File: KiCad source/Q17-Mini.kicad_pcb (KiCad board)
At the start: 2 copper layers, 95 x 75 mm, 85 parts, among them J1 Input, J2-1 SPK+, J2-2 SPK-, J3-1 V+, J3-2 GND, J3-3 V-, Q1 IRF610, Q10 KSA992, Q11 BS250P, Q12 BD139, Q13 IRF610, Q14 IRF9610, Q15 FQA46N15, Q16 FQA36P15, Q2 KSA992, Q3 KSC1845, Q4 IRF9610, Q5 FQP3P20, Q6 FQP3N30, Q7 KSC1845, Q8 ZVN4206AV, Q9 BS250P, U1 OPA1641, U1' OPA1641

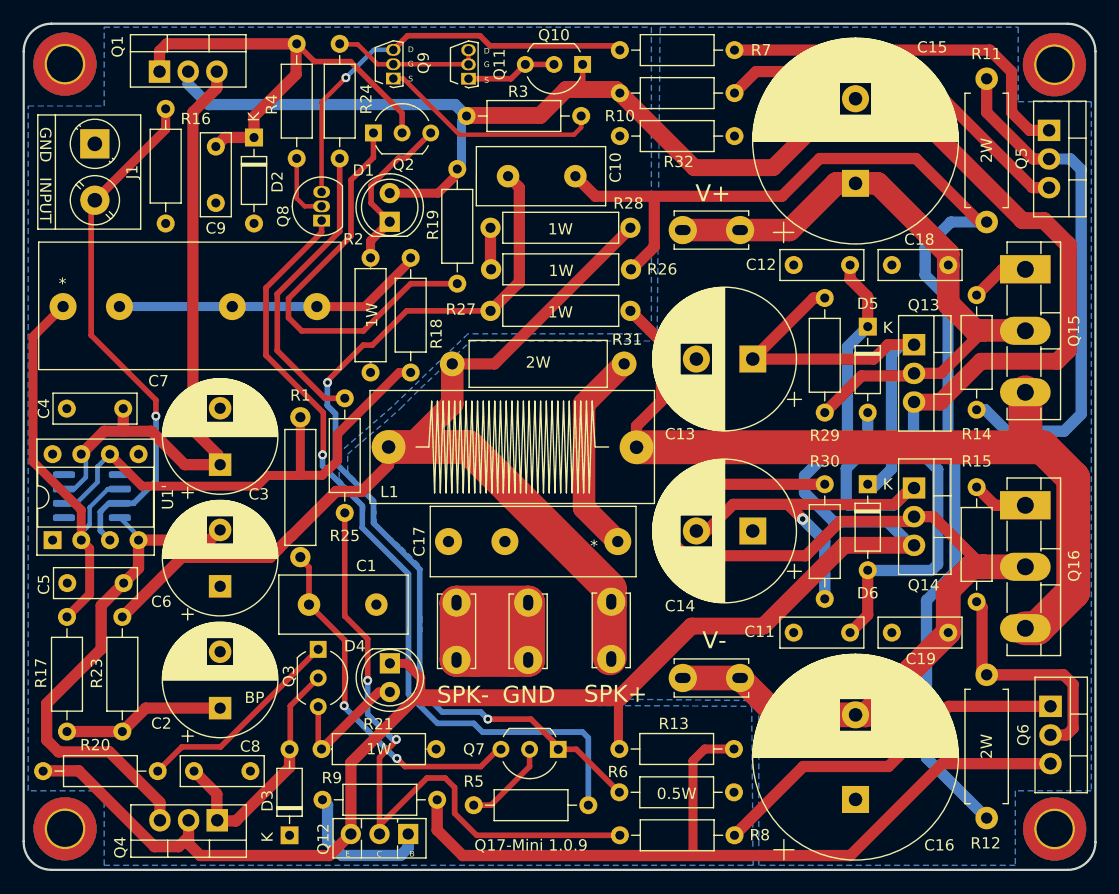
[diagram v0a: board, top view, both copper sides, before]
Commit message: PCB V1.0.9
- Add warning about DC on back PCB.
- Align ground plane.
- More reference components in schematic.
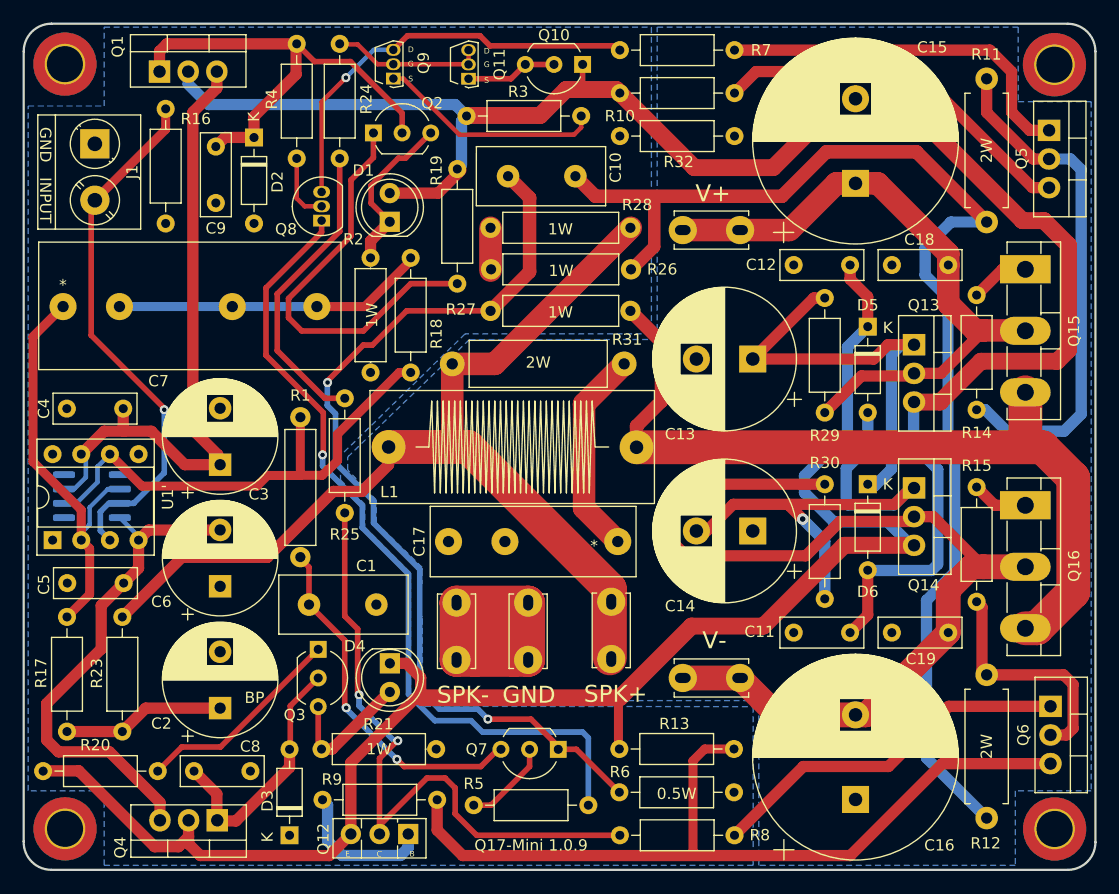
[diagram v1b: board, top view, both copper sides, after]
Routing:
- net Net-(J2-1-Pad1): track 93.3 -> 89.9 mm
- net Net-(C10-Pad2): track 82.8 -> 83.5 mm
- net Net-(C11-Pad2): track 156.5 -> 157.2 mm
- net Net-(J1-Pad2): track 46.6 -> 47.2 mm
- net Net-(C10-Pad1): track 109.4 -> 110.0 mm
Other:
- board text added: "Board not protected against DC. Use a Speaker Protection Board."

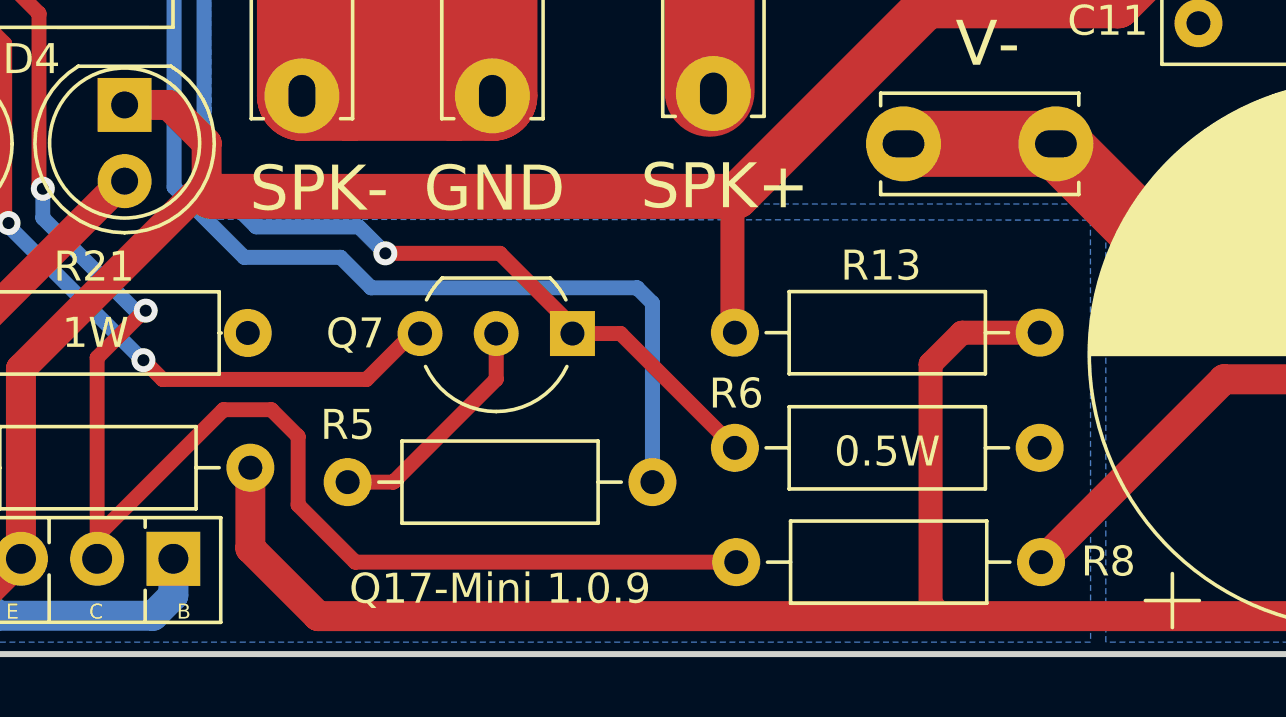
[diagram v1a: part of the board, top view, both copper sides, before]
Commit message: PCB v1.0.9
- Add a warning about DC on back of PCB.
- Some tracks optimisation.
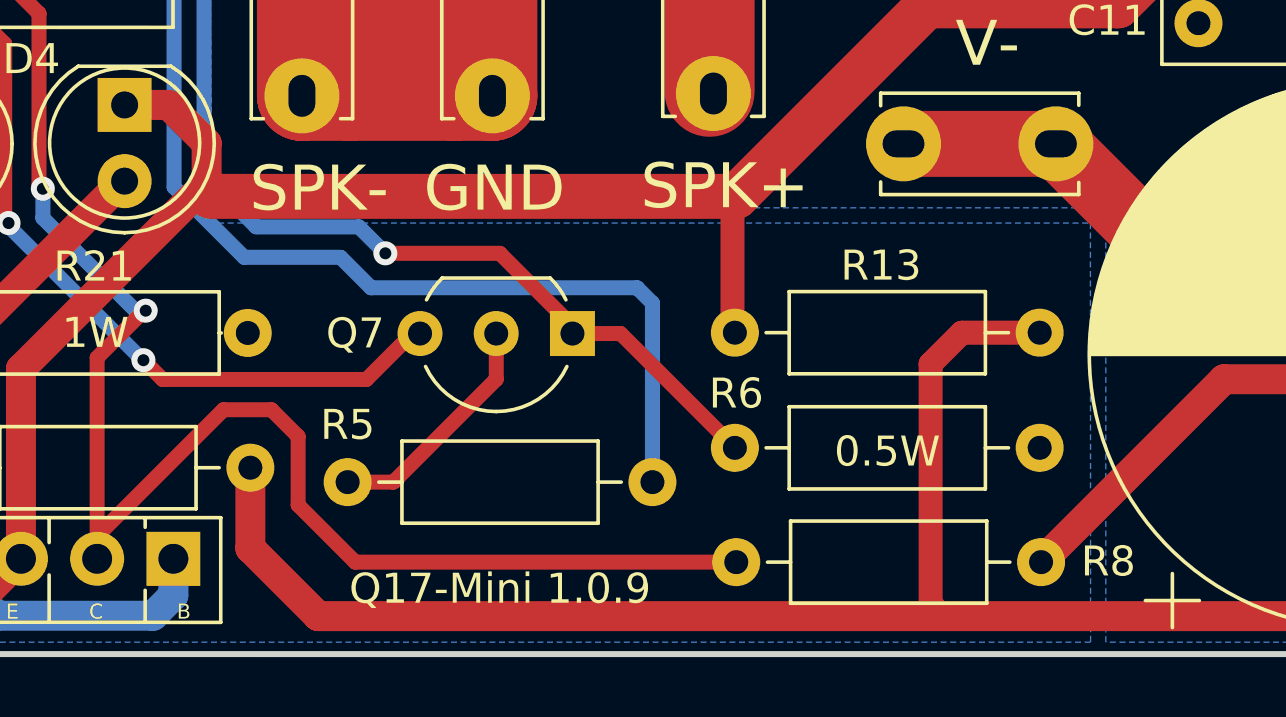
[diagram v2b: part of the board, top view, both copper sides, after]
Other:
- board text added: "Board not protected against DC."
- board text added: "Use a Speaker Protection Board or add 1uF MKP capacitor at input."
- board text removed: "Board not protected against DC. Use a Speaker Protection Board."
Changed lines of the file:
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@@
   (title_block
     (title "Q17-Mini the Quad405 reborn")
-    (date "2021-12-01")
+    (date "2021-12-05")
     (rev "1.0.9")
     (company "PCB design by Stef")
@@
     (effects (font (size 2 2) (thickness 0.25)))
   )
-  (gr_text "Board not protected against DC.\nUse a Speaker Protection Board." (at 112.649 75.692) (layer "B.SilkS")
+  (gr_text "Board not protected against DC." (at 114.5032 76.7588) (layer "B.SilkS")
+    (effects (font (size 1 0.9) (thickness 0.15)) (justify mirror))
+  )
+  (gr_text "Use a Speaker Protection Board\nor add 1uF MKP capacitor at input." (at 114.5032 83.9216) (layer "B.SilkS")
     (effects (font (size 1 0.9) (thickness 0.15)) (justify mirror))
   )
@@
         (xy 187.706 129.667)
         (xy 164.973 129.667)
-        (xy 164.972987 115.063264)
-        (xy 136.906 115.062)
+        (xy 164.972987 115.189)
+        (xy 136.906 115.189)
         (xy 135.16835 114.26215)
         (xy 135.128 107.696)
@@
         (xy 134.112 103.759)
         (xy 134.112 114.427)
-        (xy 135.382 115.57)
-        (xy 164.459613 115.599626)
+        (xy 135.382 115.697)
+        (xy 164.459613 115.697)
         (xy 164.465 129.667)
         (xy 106.934 129.667)

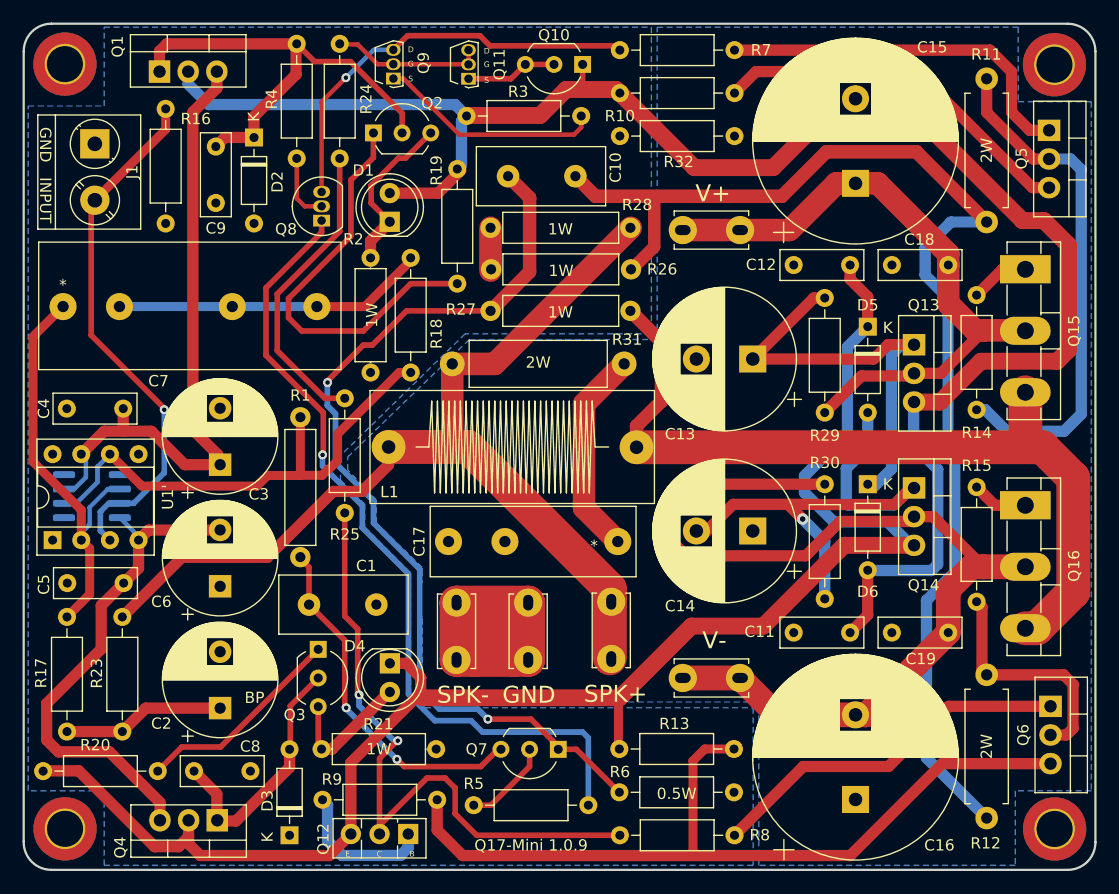
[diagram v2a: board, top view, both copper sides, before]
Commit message: PCB V1.0.9
- New footprint for CA1 (DC version).
- Enlarge tracks.
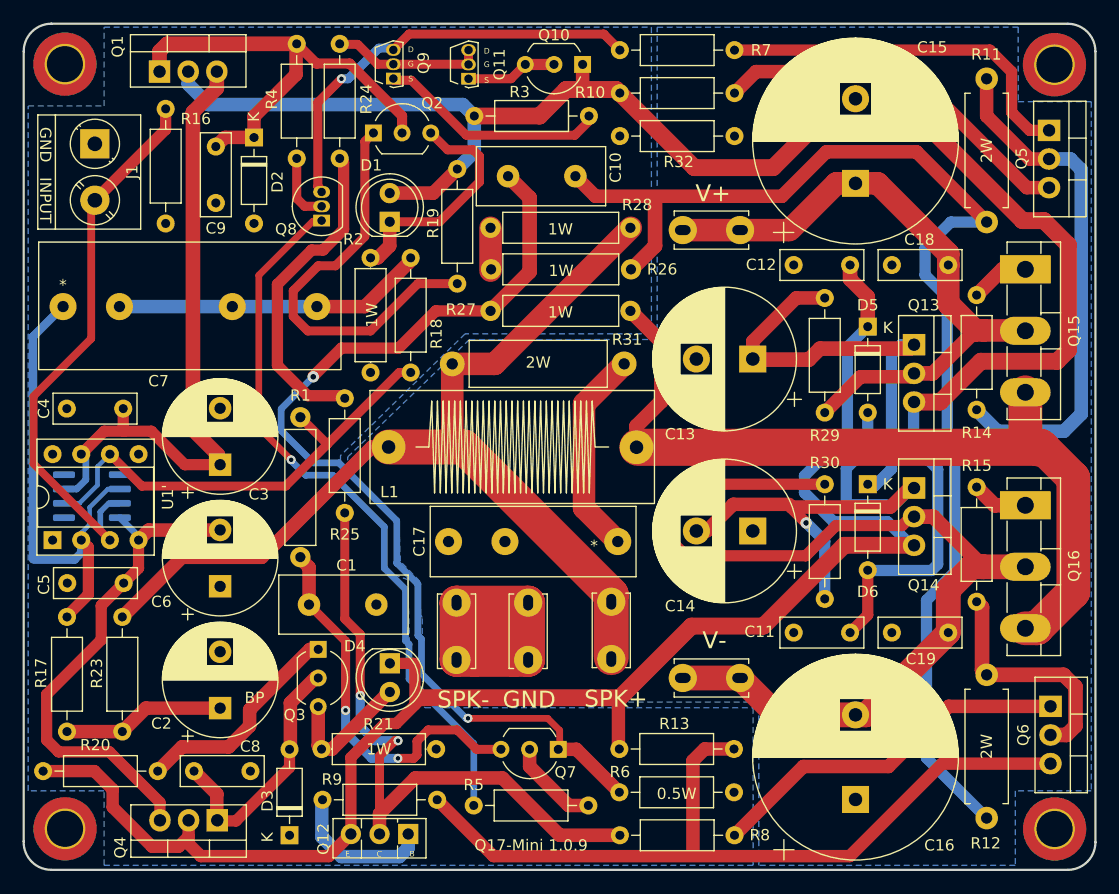
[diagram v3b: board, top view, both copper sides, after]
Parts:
- moved R5 10.2 mm to (139.7, 124.4), turned to 0 degrees
- moved R3 0.69 mm to (139.8, 63.2)
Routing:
- net Net-(Q8-Pad1): track 72.8 -> 63.8 mm
- net Net-(D1-Pad1): track 15.0 -> 21.1 mm
- net Net-(C10-Pad2): track 83.5 -> 89.2 mm
- net Net-(C7-Pad1): track 38.1 -> 43.4 mm
- net Net-(R1-Pad1): track 45.2 -> 42.2 mm
- net Net-(C1-Pad1): track 31.6 -> 34.2 mm
- net Net-(J1-Pad2): track 47.2 -> 49.6 mm, vias 1 -> 0
- net Net-(C12-Pad2): track 142.0 -> 144.1 mm
- net Net-(R24-Pad2): track 27.1 -> 28.7 mm
- net Net-(Q6-Pad3): track 73.7 -> 72.3 mm
- net Net-(Q12-Pad2): track 57.8 -> 59.0 mm
- net Net-(J2-1-Pad1): track 89.9 -> 88.8 mm
- net Net-(Q8-Pad3): track 36.8 -> 37.9 mm
- net Net-(C13-Pad1): track 38.5 -> 39.4 mm
- net Net-(Q3-Pad1): track 18.7 -> 19.5 mm

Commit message: PCB v1.0.9
New footprint for C7.
Now support 5, 7.5, 10, 15 et 22.5 mm pitch.
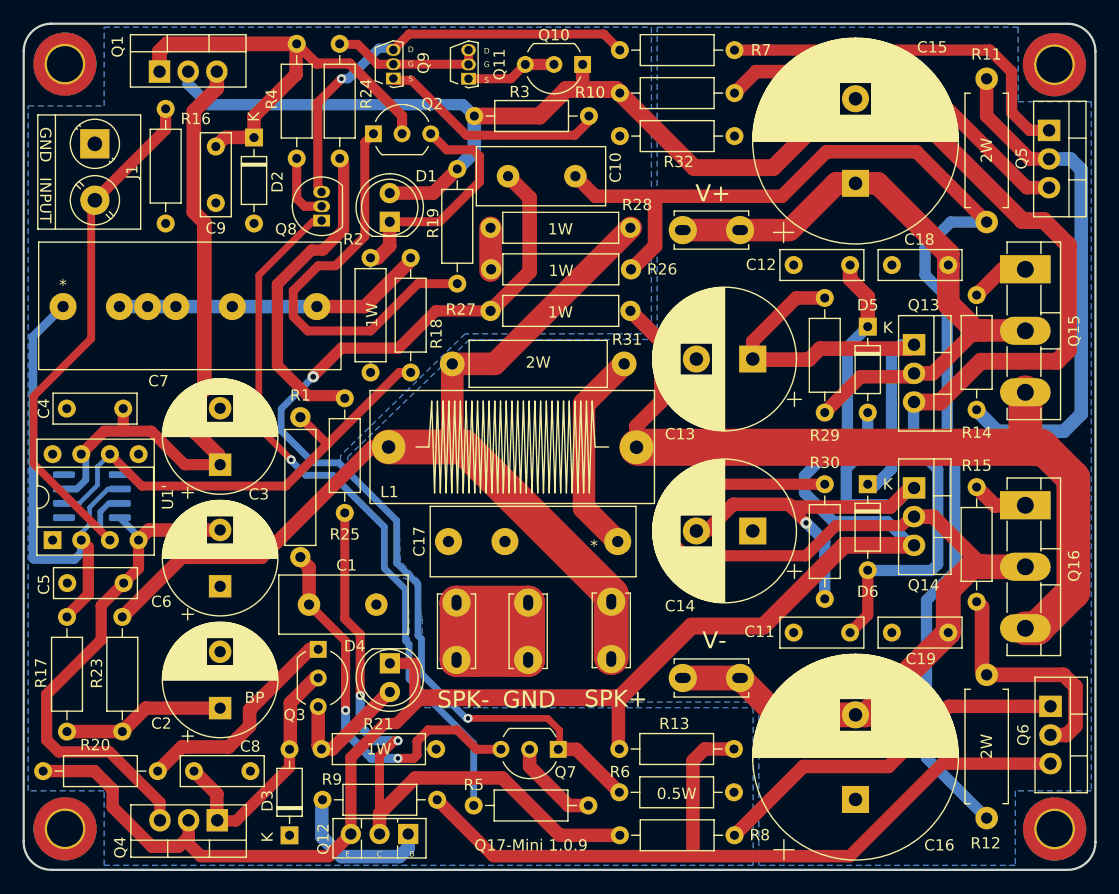
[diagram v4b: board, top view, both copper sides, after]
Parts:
- moved Q2 0.07 mm to (130.8, 64.8)
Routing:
- net Net-(C3-Pad1): track 57.2 -> 57.8 mm

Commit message: PCB V1.0.9
- New footprint for Q8, Q9 and Q11.
- Enlarge PCB holes for Faston connector.
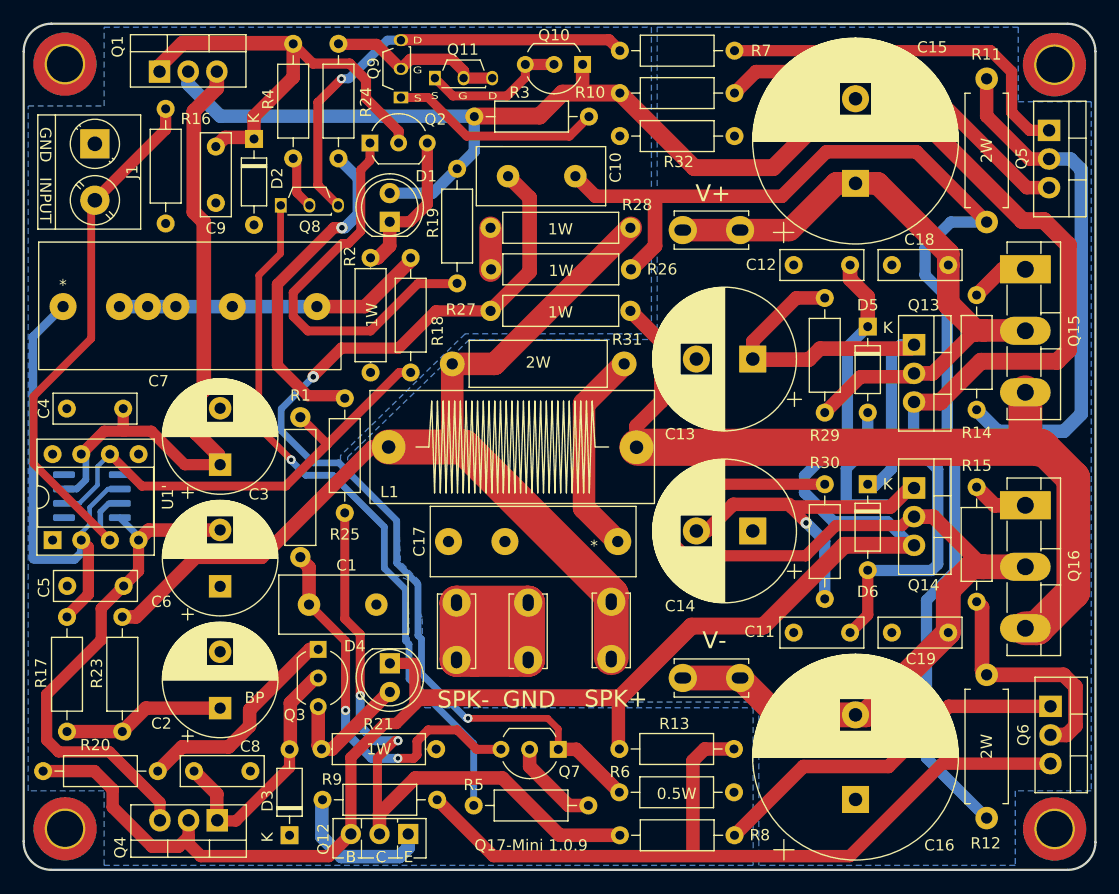
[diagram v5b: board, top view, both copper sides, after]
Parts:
- J2-1, J2-2, J3-1, J3-2, J3-3: footprint Connector_Faston:Faston_connector -> Q17_Library:Faston_Connector_63849-1_TEC
- Q11, Q9: footprint Package_TO_SOT_THT:TO-92S -> Package_TO_SOT_THT:TO-92S_Wide
- Q8: footprint Package_TO_SOT_THT:TO-92_Inline -> Package_TO_SOT_THT:TO-92S_Wide
- moved Q8 3.87 mm to (122.6, 71.2), turned to 0 degrees
- moved Q11 2.98 mm to (136.3, 59.9), turned to 0 degrees
- moved Q9 1.81 mm to (133.2, 61.6)
- moved Q2 0.87 mm to (130.5, 65.6)
- moved R4 0.31 mm to (123.7, 56.8)
- moved C5 0.25 mm to (103.7, 104.9)
- moved D2 0.13 mm to (120.2, 65.3)
- moved R24 0.11 mm to (127.7, 56.8)
- moved R3 0.05 mm to (139.8, 63.3)
- moved R7 0.05 mm to (152.7, 57.5)
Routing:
- net Net-(D1-Pad1): track 21.1 -> 13.7 mm
- net Net-(Q10-Pad2): track 7.85 -> 13.0 mm
- net Net-(Q11-Pad2): track 13.3 -> 16.0 mm
- net Net-(Q2-Pad1): track 36.8 -> 35.3 mm
- net Net-(Q9-Pad1): track 20.3 -> 18.8 mm
- net Net-(Q8-Pad3): track 37.9 -> 39.3 mm
- net Net-(Q8-Pad2): track 6.04 -> 4.62 mm
- net Net-(R24-Pad2): track 28.7 -> 29.8 mm, vias 0 -> 1
- net Net-(Q8-Pad1): track 63.8 -> 63.3 mm
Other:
- board text removed: "B"
- board text removed: "C"
- board text removed: "E"
